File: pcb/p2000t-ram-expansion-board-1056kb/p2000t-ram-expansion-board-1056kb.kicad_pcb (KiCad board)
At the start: 2 copper layers, 110 x 68.1 mm, 23 parts, among them J1 EXPANSION BOARD, J2 POWER, J3 TERMINAL, U1 74HC04, U2 AS6C4008-55PCN, U3 74HC00, U4 CY62256-70PC, U5 74HC688, U6 74HC32, U7 74HC273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

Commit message: Storing before routing
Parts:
- added REF**: OSHW-Logo2_7.3x6mm_SilkScreen, Symbol:OSHW-Logo2_7.3x6mm_SilkScreen, F.Cu at (33.0, 83.2)
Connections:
- U1 pad 1: ~{RES} -> GND
- U1 pad 10: Net-(U1-Pad10) -> unconnected-(U1-Pad10)
- U1 pad 11: S6 -> GND
- U1 pad 2: RES -> unconnected-(U1-Pad2)
- U3 pad 5: Net-(U1-Pad10) -> S6
- U7 pad 1: RES -> ~{RES}
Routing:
- net GND: track 729.4 -> 741.9 mm
- net +5V: track 517.6 -> 518.8 mm
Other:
- board text added: "0xA000-0xDFFF (2 banks x 16 kb)"
- board text added: "0xE000-0xFFFF (64 banks x 8kb)"
- board text added: "P2000T RAM EXPANSION BOARD 1M+"
- board text added: "rev0"

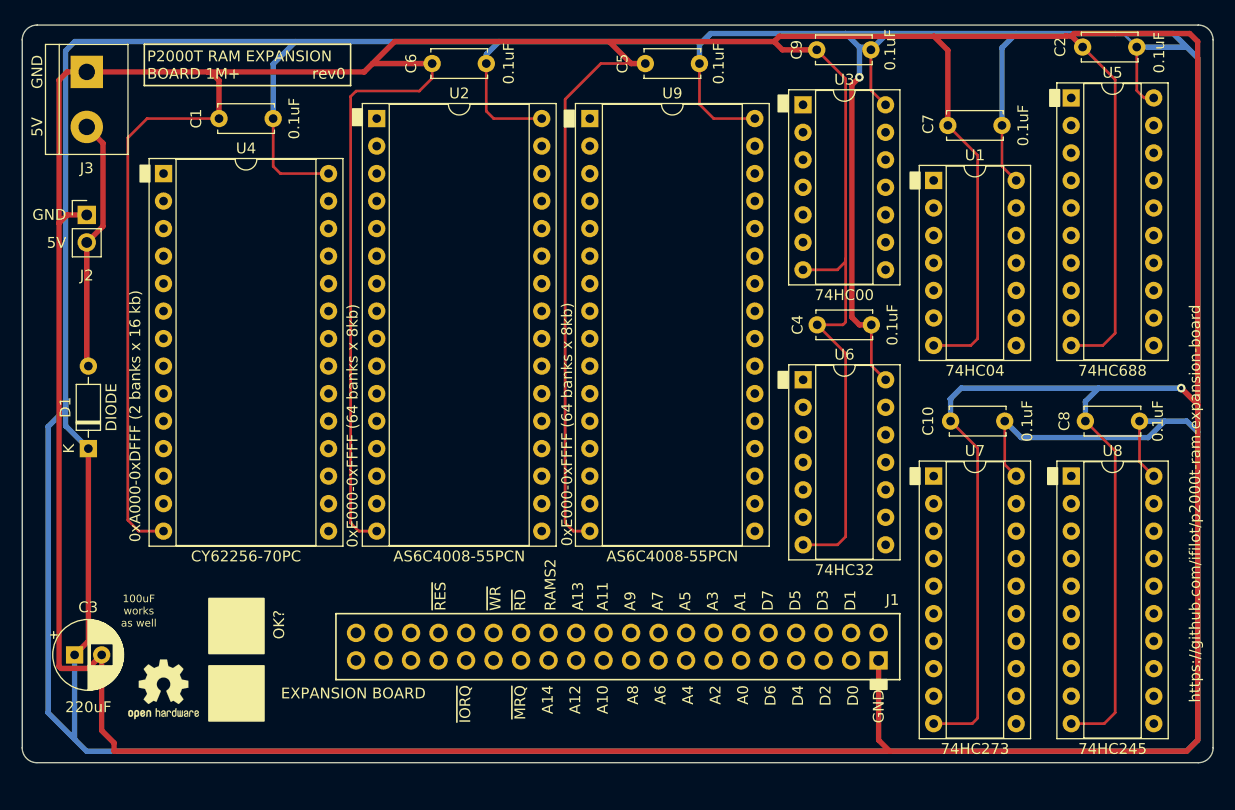
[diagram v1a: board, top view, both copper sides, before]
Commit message: Adding gerbers and SVG
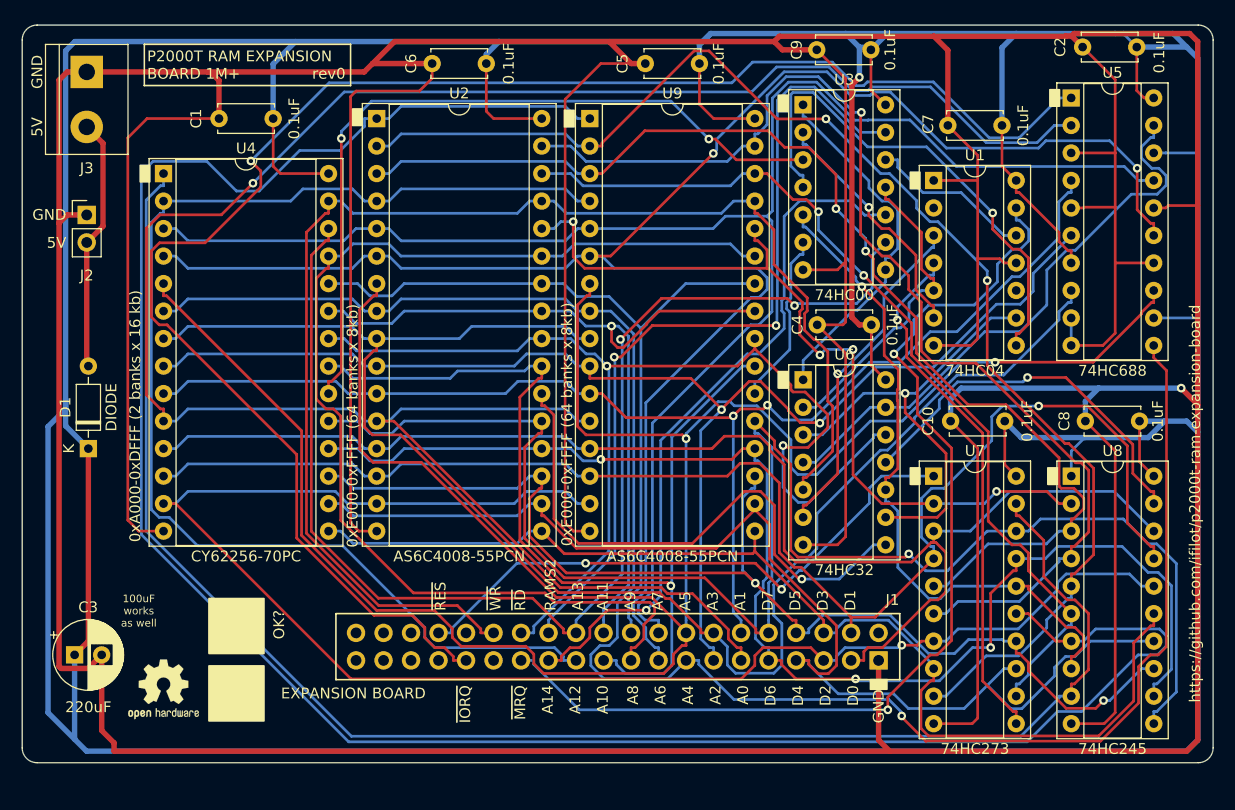
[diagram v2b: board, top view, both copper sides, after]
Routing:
- net A5: track 0.00 -> 225.8 mm, vias 0 -> 2
- net S5: track 0.00 -> 203.3 mm
- net A0: track 0.00 -> 199.3 mm, vias 0 -> 1
- net A4: track 0.00 -> 170.7 mm, vias 0 -> 1
- net A6: track 0.00 -> 170.2 mm, vias 0 -> 2
- net A7: track 0.00 -> 154.5 mm
- net ~{IORQ}: track 0.00 -> 153.1 mm, vias 0 -> 1
- net S7: track 0.00 -> 150.7 mm
- net A3: track 0.00 -> 149.2 mm
- net D7: track 0.00 -> 148.6 mm, vias 0 -> 1
- net D2: track 0.00 -> 146.0 mm, vias 0 -> 1
- net D1: track 0.00 -> 130.0 mm, vias 0 -> 1
- net ~{WR}: track 0.00 -> 125.6 mm
- net D0: track 0.00 -> 125.3 mm
- net A2: track 0.00 -> 123.6 mm, vias 0 -> 2
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
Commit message: Revising PCBs
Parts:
- removed REF**: OSHW-Logo2_7.3x6mm_SilkScreen, Symbol:OSHW-Logo2_7.3x6mm_SilkScreen
- added LOGO1: OSHW-Logo2_14.6x12mm_Copper_AND_Mask, components:OSHW-Logo2_14.6x12mm_Copper_AND_Mask, F.Cu at (39.5, 79.8)
- J1: value EXPANSION BOARD -> EXPANSION PORT
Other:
- board text added: "rev1"
- board text removed: "rev0"
